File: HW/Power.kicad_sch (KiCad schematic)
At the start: 4 parts

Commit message: Fixed board, big work in schematic, to finish
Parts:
- added C1: (no value), symbol Device:C
- added C2: (no value), symbol Device:C_Polarized
- added C3, C4, C5, C6: (no value), symbol Device:C_Small
- added D1: (no value), Diode_THT:D_DO-201AE_P15.24mm_Horizontal, symbol SMBJ20A:SMBJ20A
- added H1, H3: MH2, MountingHole:MountingHole_3.2mm_M3_Pad_TopBottom, symbol Mechanical:MountingHole_Pad
- added H2: MH3, MountingHole:MountingHole_3.2mm_M3_Pad_TopBottom, symbol Mechanical:MountingHole_Pad
- added H4: MH4, MountingHole:MountingHole_3.2mm_M3_Pad_TopBottom, symbol Mechanical:MountingHole_Pad
- added L1: (no value), symbol Device:L
- added PS1: (no value), LD90-23B24R2, symbol LD90-23B24R2:LD90-23B24R2
- added R1: (no value), symbol Device:R
- added R2, R3: (no value), symbol Device:R_Small
- added U2: (no value), symbol TS30042:TS30042
- H5: renamed from H?; value AC_fixture -> (none)
- gave numbers to parts that had none: 3
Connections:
- net GND: now also C1.2, C2.2, C3.1, D1.2 (A2), PS1.3 (-Vo), R1.2, R3.2, U2.14 (PGND), U2.15 (PGND), U2.17 (PAD), U2.4 (GND), U2.6 (NC), U2.7 (NC)
- net LIVE: now also PS1.2 (AC/L)
- net NEUTRAL: now also PS1.1 (AC/N)
- net +24V: now reaches SW1.2 (B)
- net +24V: now also C3.2, U2.11 (VCC), U2.2 (VCC), U2.3 (VCC)
- net +12V: no longer names the net of SW1.1 (A)
- net +12V: now also C1.1, C2.1, D1.1 (A1), PS1.4 (+Vo), R1.1
- new net: C4.1, U2.10 (BST)
- new net: C4.2, L1.1, U2.1 (VSW), U2.12 (VSW), U2.13 (VSW), U2.16 (VSW)
- new net: R2.2, R3.1, U2.5 (FB)
- new net +3V3: C5.2, C6.2, L1.2, R2.1
- new net PGND: C5.1, C6.1
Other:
- note added: "- 3.75A @ 24V = 90W, integrated slow-blow fuse"
- note added: "-Vout = 0.9*(1 + Rtop/Rbottom) -For the ADJ version, Vcc/Vout cannot exceed 16, 7.2727 in this case"
- note added: "3.3V regulator"
- note added: "Mounting Holes"
- note removed: "Note: 5 A max current (60 W)"
- moved on the sheet: H5, H6, H7, SW1

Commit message: Finished sch, to be checked. Initial components layout
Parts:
- removed PS1: (no value), LD90-23B24R2, symbol LD90-23B24R2:LD90-23B24R2
- removed SW1: MAIN_SWITCH, symbol Switch:SW_SPST
- added D2: RED, LED_SMD:LED_0603_1608Metric, symbol Device:LED
- added H8, H9: AC_LIVE, MountingHole:MountingHole_2.2mm_M2_Pad_TopBottom, symbol Mechanical:MountingHole_Pad
- added PS1: LD90-23B12R2, symbol LD90-23B24R2:LD90-23B12R2
- added R8: 1k, Resistor_SMD:R_0603_1608Metric, symbol Device:R_Small
- C1: value (none) -> 1uF
- C2: value (none) -> 200uF
- C3: value (none) -> 10uF; footprint (none) -> Capacitor_SMD:C_0603_1608Metric
- C4: value (none) -> 22nF; footprint (none) -> Capacitor_SMD:C_0603_1608Metric
- C5, C6: value (none) -> 22u; footprint (none) -> Capacitor_SMD:C_0603_1608Metric
- D1: value (none) -> SMBJ20A; footprint Diode_THT:D_DO-201AE_P15.24mm_Horizontal -> (none)
- H5: value (none) -> AC_cable_fixture
- L1: value (none) -> 4u7
- R1: value (none) -> BR_DNP; footprint (none) -> Resistor_SMD:R_1210_3225Metric
- R2: value (none) -> 10k; footprint (none) -> Resistor_SMD:R_0603_1608Metric
- R3: value (none) -> 3750; footprint (none) -> Resistor_SMD:R_0603_1608Metric
- U2: value (none) -> TS30042-M000QFNR; footprint (none) -> Package_DFN_QFN:QFN-16-1EP_3x3mm_P0.5mm_EP1.75x1.75mm_ThermalVias
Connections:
- net +3V3: now also R8.2
- net GND: now also D2.1 (K), PS1.3 (-Vo)
- net LIVE: now also PS1.2 (AC/L)
- net NEUTRAL: now also PS1.1 (AC/N)
- net at C1.1, C2.1, D1.1 (A1)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: now also H8.1, PS1.4 (+Vo)
- net +24V renamed +12V
- net +12V: now also H9.1
- new net: D2.2 (A), R8.1
- no-connect marks 0 -> 2
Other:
- note added: "- 6.7A @ 12V = 80W, integrated slow-blow fuse"
- note removed: "- 3.75A @ 24V = 90W, integrated slow-blow fuse"
- moved on the sheet: C1, C2, C3, C4, C5, C6, D1, H1, H2, H3, H4, H5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

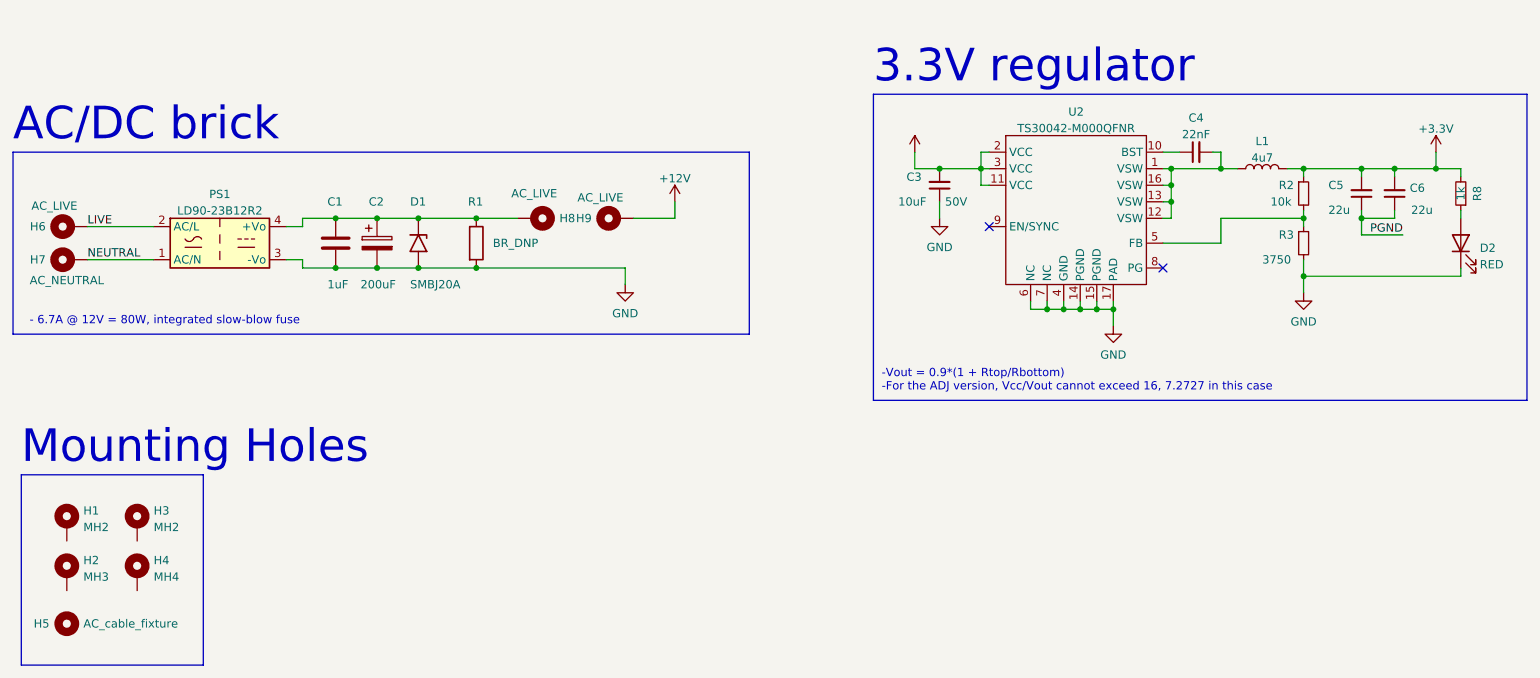
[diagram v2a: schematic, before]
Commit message: Sch finalized, added EMC stuff, user buttons and oled
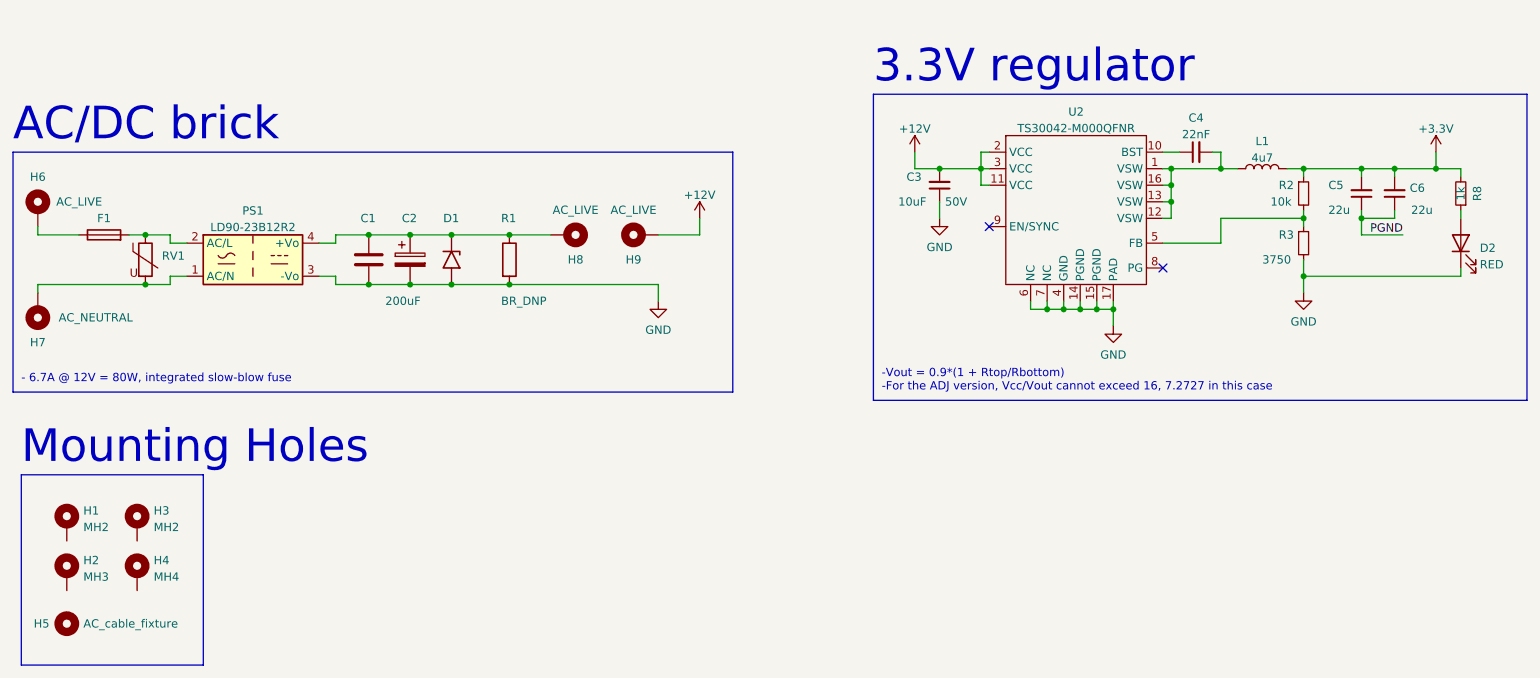
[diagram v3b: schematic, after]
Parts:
- added F1: (no value), symbol Device:Fuse
- added RV1: (no value), symbol Device:Varistor
- C1: value 1uF -> (none); footprint (none) -> Capacitor_SMD:C_1206_3216Metric
- C2: footprint (none) -> Capacitor_THT:CP_Radial_D10.0mm_P5.00mm
- D1: value SMBJ20A -> (none); footprint (none) -> Diode_SMD:D_SMB
- L1: footprint (none) -> BWVS005050404R7M00:BWVS005050404R7M00
- PS1: footprint (none) -> LD90-23B12R2:LD90-23B12R2
- R1: footprint Resistor_SMD:R_1210_3225Metric -> (none)
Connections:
- net LIVE: no longer names the net of PS1.2 (AC/L)
- net LIVE: now also F1.2, RV1.1; no longer H6.1
- net NEUTRAL: no longer names the net of H7.1, PS1.1 (AC/N)
- net NEUTRAL: now also RV1.2
- new net: F1.1, H6.1
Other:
- moved on the sheet: C1, C2, D1, H6, H7, H8, H9, PS1, R1

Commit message: Work on layout, sch fixes, added several 3d models
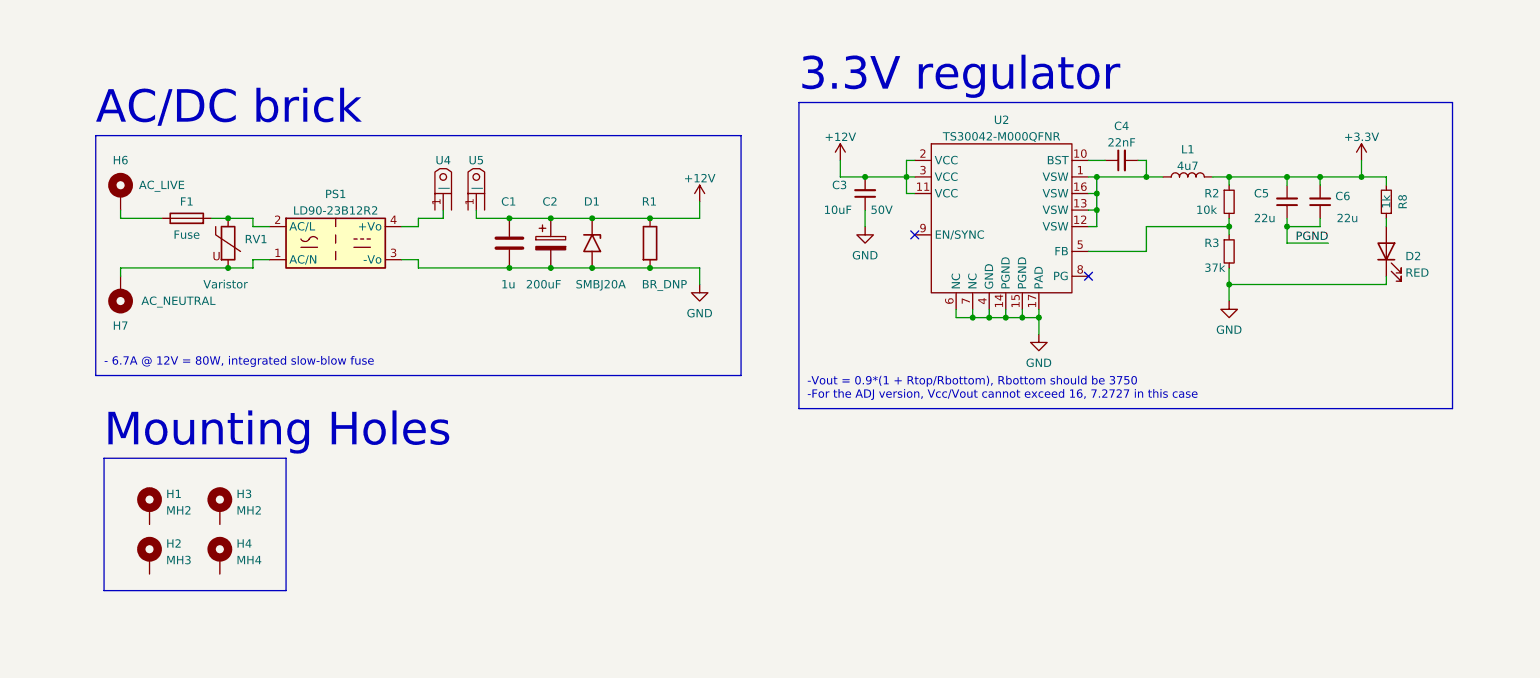
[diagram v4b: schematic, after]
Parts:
- removed H5: AC_cable_fixture, MountingHole:MountingHole_3.2mm_M3_Pad_TopBottom, symbol Mechanical:MountingHole
- removed H8, H9: AC_LIVE, MountingHole:MountingHole_2.2mm_M2_Pad_TopBottom, symbol Mechanical:MountingHole_Pad
- added U4, U5: fork_p5.0mm, fork_connector_p5.0mm:fork_p5.0mm, symbol fork_press_connector:fork_p5.0mm
- C1: value (none) -> 1u
- D1: value (none) -> SMBJ20A
- F1: value (none) -> Fuse
- R1: footprint (none) -> Resistor_SMD:R_2010_5025Metric
- R3: value 3750 -> 37k
- RV1: value (none) -> Varistor
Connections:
- net +12V: now also C1.1, C2.1, D1.1 (A1), R1.1, U5.1 (|)
- new net: PS1.4 (+Vo), U4.1 (|)
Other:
- note added: "-Vout = 0.9*(1 + Rtop/Rbottom), Rbottom should be 3750 -For the ADJ version, Vcc/Vout cannot exceed 16, 7.2727 in this case"
- note removed: "-Vout = 0.9*(1 + Rtop/Rbottom) -For the ADJ version, Vcc/Vout cannot exceed 16, 7.2727 in this case"
- moved on the sheet: C1, C2, C3, C4, C5, C6, D1, D2, F1, H1, H2, H3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

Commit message: starterd routing, removed OTG usb port
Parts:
- removed H1: MH2, MountingHole:MountingHole_3.2mm_M3_Pad_TopBottom, symbol Mechanical:MountingHole_Pad
- removed H4: MH4, MountingHole:MountingHole_3.2mm_M3_Pad_TopBottom, symbol Mechanical:MountingHole_Pad
- added C12: 100n, Capacitor_SMD:C_0603_1608Metric, symbol Device:C_Small
- F1: footprint (none) -> 3622_fuse_holder:3622
- RV1: footprint (none) -> B72214S0351K101:B72214S0351K101
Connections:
- net PGND is gone; now on net GND: C5.1, C6.1
- net +12V: now also C12.2
- net GND: now also C12.1; no longer U2.6 (NC), U2.7 (NC)
- no-connect marks 2 -> 4
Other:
- moved on the sheet: C3, C4, C5, C6, D2, L1, R2, R3, R8, U2

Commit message: Finished routing, only mosfet left, fixed layout, outline
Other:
- moved on the sheet: H2
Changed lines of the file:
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@@
     (stroke (width 0) (type default) (color 0 0 0 0))
   )
-  (polyline (pts (xy 73.66 144.78) (xy 73.66 124.46))
+  (polyline (pts (xy 73.66 138.43) (xy 73.66 124.46))
     (stroke (width 0) (type default) (color 0 0 0 0))
   )
@@
     (stroke (width 0) (type default) (color 0 0 0 0))
   )
-  (polyline (pts (xy 45.72 144.78) (xy 73.66 144.78))
+  (polyline (pts (xy 45.72 138.43) (xy 73.66 138.43))
     (stroke (width 0) (type default) (color 0 0 0 0))
   )
@@
     (stroke (width 0) (type default) (color 0 0 0 0))
   )
-  (polyline (pts (xy 45.72 124.46) (xy 45.72 144.78))
+  (polyline (pts (xy 45.72 124.46) (xy 45.72 138.43))
     (stroke (width 0) (type default) (color 0 0 0 0))
   )
@@
     (pin "1")
   )
-  (symbol (lib_id "Mechanical:MountingHole_Pad") (at 52.705 139.7 0) (unit 1)
-    (in_bom yes) (on_board yes) (fields_autoplaced)
-    (property "Reference" "H2" (id 0) (at 55.245 137.5953 0)
-      (effects (font (size 1.27 1.27)) (justify left))
-    )
-    (property "Value" "MH3" (id 1) (at 55.245 140.1322 0)
-      (effects (font (size 1.27 1.27)) (justify left))
-    )
-    (property "Footprint" "MountingHole:MountingHole_3.2mm_M3_Pad_TopBottom" (id 2) (at 52.705 139.7 0)
-      (effects (font (size 1.27 1.27)) hide)
-    )
-    (property "Datasheet" "~" (id 3) (at 52.705 139.7 0)
-      (effects (font (size 1.27 1.27)) hide)
-    )
+  (symbol (lib_id "Mechanical:MountingHole_Pad") (at 52.07 132.08 0) (unit 1)
+    (in_bom yes) (on_board yes) (fields_autoplaced)
+    (property "Reference" "H2" (id 0) (at 54.61 129.9753 0)
+      (effects (font (size 1.27 1.27)) (justify left))
+    )
+    (property "Value" "MH3" (id 1) (at 54.61 132.5122 0)
+      (effects (font (size 1.27 1.27)) (justify left))
+    )
+    (property "Footprint" "MountingHole:MountingHole_3.2mm_M3_Pad_TopBottom" (id 2) (at 52.07 132.08 0)
+      (effects (font (size 1.27 1.27)) hide)
+    )
+    (property "Datasheet" "~" (id 3) (at 52.07 132.08 0)
+      (effects (font (size 1.27 1.27)) hide)
+    )

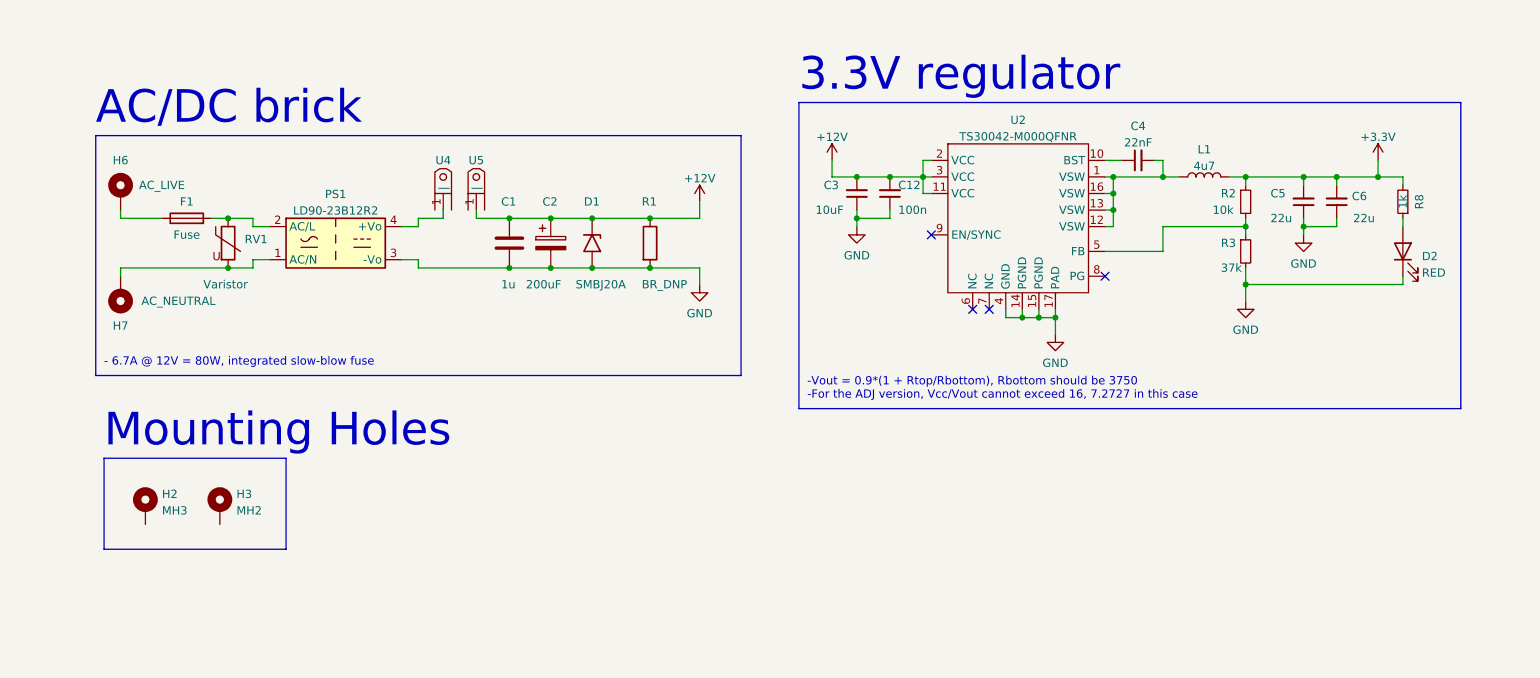
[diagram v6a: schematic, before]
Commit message: QOL changes on pcb, fixed wrong ACDC brick polarity xD
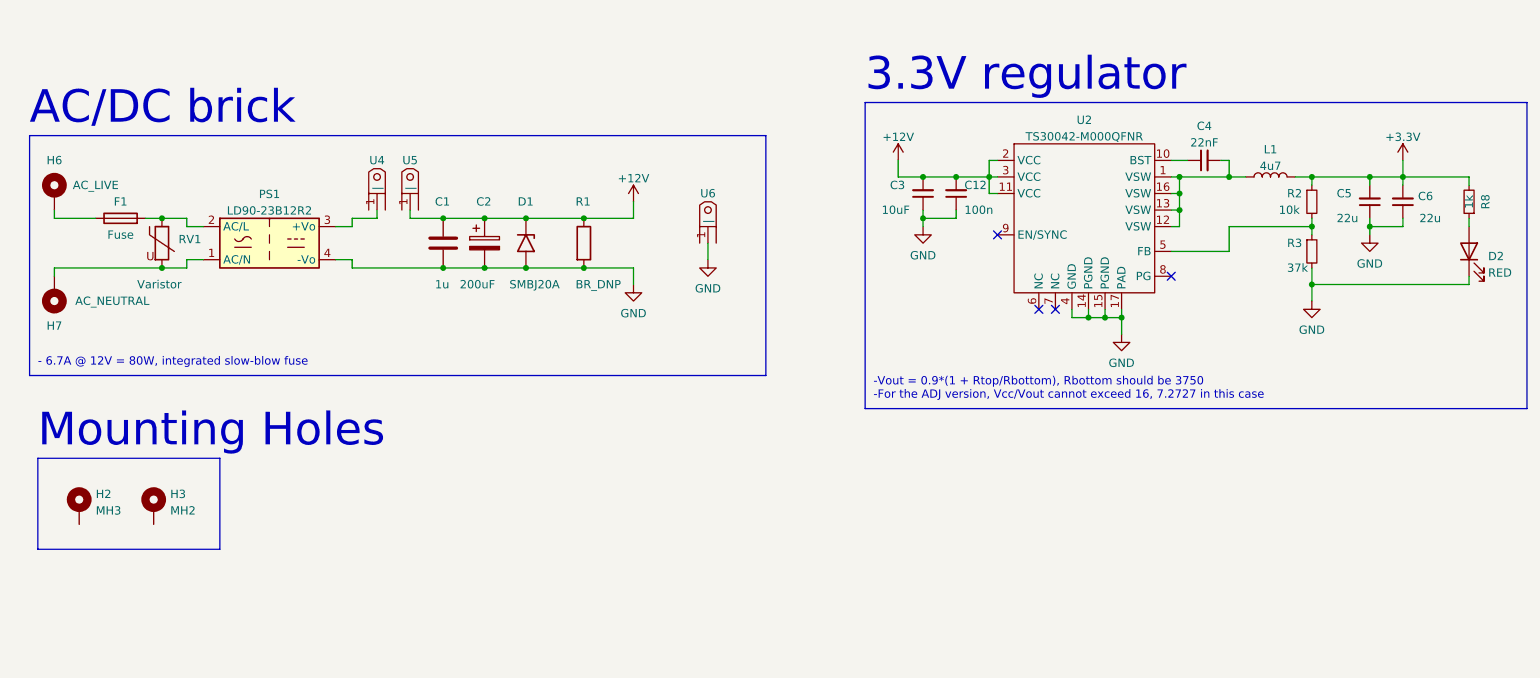
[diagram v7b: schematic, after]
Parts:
- added U6: fork_p5.0mm, fork_connector_p5.0mm:fork_p5.0mm, symbol fork_press_connector:fork_p5.0mm
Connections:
- net GND: now also PS1.4 (-Vo), U6.1 (|); no longer PS1.3 (-Vo)
- net at U4.1 (|): now also PS1.3 (+Vo); no longer PS1.4 (+Vo)
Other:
- moved on the sheet: C1, C12, C2, C3, C4, C5, C6, D1, D2, F1, H2, H3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

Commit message: revision 0
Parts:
- C2: value 200uF -> 200u
- C4: value 22nF -> 22n
- R1: value BR_DNP -> DNP
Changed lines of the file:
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@@
     (in_bom yes) (on_board yes) (fields_autoplaced)
     (property "Reference" "C4" (id 0) (at 214.6363 73.4781 90))
-    (property "Value" "22nF" (id 1) (at 214.6363 76.015 90))
+    (property "Value" "22n" (id 1) (at 214.6363 76.015 90))
     (property "Footprint" "Capacitor_SMD:C_0603_1608Metric" (id 2) (at 214.63 78.74 0)
       (effects (font (size 1.27 1.27)) hide)
@@
       (effects (font (size 1.27 1.27)) (justify left))
     )
-    (property "Value" "BR_DNP" (id 1) (at 118.11 97.79 0)
+    (property "Value" "DNP" (id 1) (at 118.11 97.79 0)
       (effects (font (size 1.27 1.27)) (justify left))
     )
@@
       (effects (font (size 1.27 1.27)) (justify left))
     )
-    (property "Value" "200uF" (id 1) (at 100.33 97.79 0)
-      (effects (font (size 1.27 1.27)) (justify left))
-    )
+    (property "Value" "200u" (id 1) (at 101.6 97.79 0)
+      (effects (font (size 1.27 1.27)) (justify left))
+    )
